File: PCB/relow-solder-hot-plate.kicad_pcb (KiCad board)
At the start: 2 copper layers, 100 x 100 mm, 57 parts, among them J1 Barrel_Jack_Switch, Q1 WSP4409A, Q2 IRLR8726TRPBF, Q3 SS8050, SW1 SW_Push, SW2 SW_Push, U1 ATMEGA4809-AFR, U2 AMS1117-5.0

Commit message: layout done
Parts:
- removed D4: B5819W, Diode_SMD:D_SOD-123
- removed LED1: RED/GREEN, LED_SMD:LED_Avago_PLCC4_3.2x2.8mm_CW
- removed OLED1: SSD1306, User:0.91Inch-OLED-Module
- removed R10: 4k7, Resistor_SMD:R_0805_2012Metric
- removed SW2: SW_Push, Button_Switch_THT:SW_PUSH_6mm
- removed TEMP3: Ext. 1-Wire, Connector_PinHeader_2.54mm:PinHeader_1x03_P2.54mm_Vertical
- removed UPDI1: 1x03_2.54mm, Connector_PinHeader_2.54mm:PinHeader_1x03_P2.54mm_Vertical
- added L1: 4.7u, Inductor_SMD:L_1210_3225Metric, F.Cu at (116.2, 68.2)
- added R16: 1K, Resistor_SMD:R_0603_1608Metric, F.Cu at (147.7, 65.8)
- added U3: ESP32-S3-MINI-1, Espressif:ESP32-S3-MINI-1, F.Cu at (131.6, 70.2)
- C1: value 10u -> 100n; footprint Capacitor_SMD:C_0805_2012Metric -> Capacitor_SMD:C_0603_1608Metric
- C10: value 100nF -> 10u; footprint Capacitor_SMD:C_0805_2012Metric -> Capacitor_SMD:C_0603_1608Metric
- C11, C12, C9: value 100nF -> 100n; footprint Capacitor_SMD:C_0805_2012Metric -> Capacitor_SMD:C_0603_1608Metric
- C13: value 100nF -> 68p; footprint Capacitor_SMD:C_0805_2012Metric -> Capacitor_SMD:C_0603_1608Metric
- C2: value 680u/16V -> 10u; footprint Capacitor_THT:CP_Radial_D8.0mm_P3.50mm -> Capacitor_SMD:C_0603_1608Metric
- C6: value 22u/16V -> 680u/16V; footprint Capacitor_SMD:CP_Elec_4x5.4 -> Capacitor_THT:CP_Radial_D8.0mm_P3.50mm
- C7: value 22u/16V -> 10u; footprint Capacitor_SMD:CP_Elec_4x5.4 -> Capacitor_SMD:C_0603_1608Metric
- C8: value 470pF -> 10u; footprint Capacitor_SMD:C_0805_2012Metric -> Capacitor_SMD:C_0603_1608Metric
- D3: value B5819W -> LED_RBAG; footprint Diode_SMD:D_SOD-123 -> LED_SMD:LED_Cree-PLCC4_2x2mm_CW
- F1: value 5A -> 3A
- J1: value Barrel_Jack_Switch -> USB_C_Receptacle; footprint Connector_BarrelJack:BarrelJack_Horizontal -> Connector_USB:USB_C_Receptacle_HRO_TYPE-C-31-M-12
- R1, R2: value 47 -> 100K; footprint Resistor_SMD:R_0805_2012Metric -> Resistor_SMD:R_0603_1608Metric
- R11: footprint Resistor_SMD:R_0805_2012Metric -> Resistor_SMD:R_0603_1608Metric
- R12: value 10k -> 1k; footprint Resistor_SMD:R_0805_2012Metric -> Resistor_SMD:R_0603_1608Metric
- R13: value 10k -> 10K; footprint Resistor_SMD:R_0805_2012Metric -> Resistor_SMD:R_0603_1608Metric
- R14, R15: value 10k -> 1K; footprint Resistor_SMD:R_0805_2012Metric -> Resistor_SMD:R_0603_1608Metric
- R3: value 1k -> 10K; footprint Resistor_SMD:R_0805_2012Metric -> Resistor_SMD:R_0603_1608Metric
- R4: value 4k7 -> 22K; footprint Resistor_SMD:R_0805_2012Metric -> Resistor_SMD:R_0603_1608Metric
- R5, R6: value 1k -> 5K1; footprint Resistor_SMD:R_0805_2012Metric -> Resistor_SMD:R_0603_1608Metric
- R7: value 1k -> 200K; footprint Resistor_SMD:R_0805_2012Metric -> Resistor_SMD:R_0603_1608Metric
- R8: value 4k7 -> 1K; footprint Resistor_SMD:R_0805_2012Metric -> Resistor_SMD:R_0603_1608Metric
- R9: value 4k7 -> 5K1; footprint Resistor_SMD:R_0805_2012Metric -> Resistor_SMD:R_0603_1608Metric
- SW1: footprint Button_Switch_THT:SW_PUSH_6mm -> Button_Switch_THT:SW_PUSH_6mm_H4.3mm
- TEMP2: value DS18B20Z -> LMT85; footprint Package_SO:SOIC-8_3.9x4.9mm_P1.27mm -> Package_SO:Texas_R-PDSO-N5
- U1: value ATMEGA4809-AFR -> DIO6912; footprint Package_QFP:TQFP-48_7x7mm_P0.5mm -> Package_TO_SOT_SMD:SOT-23-6
- U2: value AMS1117-5.0 -> IP2721; footprint Package_TO_SOT_SMD:SOT-89-3 -> Package_SO:TSSOP-16_4.4x5mm_P0.65mm
- moved R7 95.5 mm to (62.6, 69.6)
- moved R6 90.6 mm to (64.2, 73.0), turned to 90 degrees
- moved R5 66.2 mm to (62.6, 73.0), turned to 90 degrees
- moved R2 56.2 mm to (120.6, 62.8), turned to 90 degrees
- moved C1 53.6 mm to (115.4, 65.6), turned to 0 degrees
- moved U2 53.1 mm to (72.0, 74.0), turned to 180 degrees
- moved R11 48.3 mm to (110.6, 71.6), turned to 0 degrees
- moved R3 48.0 mm to (65.8, 69.6), turned to -90 degrees
- moved C6 30.6 mm to (88.1, 66.3), turned to 90 degrees
- moved C13 28.7 mm to (155.8, 94.0), turned to 180 degrees
- moved R13 28.4 mm to (150.8, 75.6), turned to 90 degrees
- moved D3 24.7 mm to (149.2, 62.5), turned to 180 degrees
- moved C2 23.9 mm to (64.2, 69.6)
- moved C8 22.0 mm to (119.8, 68.2), turned to 90 degrees
- moved U1 19.6 mm to (116.0, 63.0), turned to 180 degrees
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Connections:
- C10 pad 1: /SW_UP -> GND
- C10 pad 2: GND -> +3V3
- C11 pad 1: +5V -> GND
- C11 pad 2: GND -> +3V3
- C12 pad 1: /SW_DN -> GND
- C12 pad 2: GND -> /GPIO_0/BOOT
- C13 pad 1: +5V -> GND
- C13 pad 2: GND -> /T_ANALOG
- C2 pad 1: VCC -> Net-(C2-Pad1)
- C2 pad 2: GND -> Net-(C2-Pad2)
- C6 pad 1: Net-(C6-Pad1) -> VCC
- C7 pad 1: +5V -> GND
- C7 pad 2: GND -> Net-(C7-Pad2)
- C8 pad 1: /TDATA_A -> GND
- C8 pad 2: GND -> +3V3
- C9 pad 1: +5V -> GND
- C9 pad 2: GND -> Net-(C9-Pad2)
- D1 pad 1: Net-(C6-Pad1) -> Net-(C7-Pad2)
- D3 pad 1: Net-(C6-Pad1) -> Net-(D3-Pad1)
- D3 pad 2: +5V -> Net-(D3-Pad2)
- F1 pad 2: Net-(C1-Pad1) -> Net-(C2-Pad2)
- Q1 pad 4: Net-(C1-Pad2) -> Net-(C2-Pad1)
- Q1 pad 5: Net-(C1-Pad1) -> Net-(C2-Pad2)
- Q1 pad 6: Net-(C1-Pad1) -> Net-(C2-Pad2)
- Q1 pad 7: Net-(C1-Pad1) -> Net-(C2-Pad2)
- Q1 pad 8: Net-(C1-Pad1) -> Net-(C2-Pad2)
- R1 pad 1: Net-(J1-Pad3) -> VCC
- R1 pad 2: Net-(C1-Pad1) -> /SEL
- R11 pad 1: Net-(C1-Pad2) -> Net-(Q3-Pad1)
- R11 pad 2: GND -> +3V3
- R12 pad 1: Net-(C6-Pad1) -> /GATE
- R12 pad 2: /VCC-DIV -> Net-(Q3-Pad1)
- R13 pad 1: Net-(Q3-Pad1) -> +3V3
- R13 pad 2: +5V -> /GPIO_0/BOOT
- R14 pad 1: /SW_UP -> /LED_R
- R14 pad 2: +5V -> Net-(D3-Pad1)
- R15 pad 1: /SW_DN -> Net-(D3-Pad4)
- R15 pad 2: +5V -> /LED_G
- R2 pad 1: Net-(J1-Pad3) -> +3V3
- R2 pad 2: VCC -> Net-(R2-Pad2)
- R3 pad 1: /VCC-DIV -> Net-(C2-Pad2)
- R4 pad 1: Net-(Q2-Pad1) -> Net-(R2-Pad2)
- R4 pad 2: VCC -> GND
- R5 pad 1: /GATE -> /CC1
- R5 pad 2: Net-(Q3-Pad1) -> GND
- R6 pad 1: /LED_G -> /CC2
- R6 pad 2: Net-(LED1-Pad3) -> GND
- R7 pad 1: /LED_R -> Net-(C2-Pad1)
- R7 pad 2: Net-(LED1-Pad1) -> GND
- R8 pad 1: +5V -> Net-(C9-Pad2)
- R8 pad 2: /I2C_SDA -> +3V3
- R9 pad 1: +5V -> VCC
- R9 pad 2: /I2C_SCL -> Net-(Q2-Pad1)
- SW1 pad 1: /SW_UP -> /GPIO_0/BOOT
- TEMP1 pad 1: +5V -> +3V3
- TEMP1 pad 2: /TDATA_A -> /T_ANALOG
- TEMP2 pad 1: unconnected-(TEMP2-Pad1) -> +3V3
- TEMP2 pad 2: unconnected-(TEMP2-Pad2) -> /T_ANALOG
- TEMP2 pad 3: +5V -> GND
- TEMP2 pad 4: /TDATA_D -> (no net)
- TEMP2 pad 5: GND -> (no net)
- U1 pad 1: unconnected-(U1-Pad1) -> Net-(C1-Pad2)
- U1 pad 2: unconnected-(U1-Pad2) -> GND
- U1 pad 3: unconnected-(U1-Pad3) -> Net-(R2-Pad2)
- U1 pad 4: unconnected-(U1-Pad4) -> Net-(C7-Pad2)
- U1 pad 5: unconnected-(U1-Pad5) -> Net-(C7-Pad2)
- U1 pad 6: unconnected-(U1-Pad6) -> Net-(C1-Pad1)
- U2 pad 1: GND -> unconnected-(U2-Pad1)
- U2 pad 2: +5V -> VCC
- U2 pad 3: Net-(C6-Pad1) -> unconnected-(U2-Pad3)
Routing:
- net +5V: track 131.9 -> 0.00 mm, vias 2 -> 0
- net +3V3: track 0.00 -> 73.0 mm
- net /D+: track 0.00 -> 65.1 mm, vias 0 -> 2
- net /D-: track 0.00 -> 62.6 mm, vias 0 -> 2
- net /T_ANALOG: track 0.00 -> 59.0 mm
- net /TDATA_D: track 55.1 -> 0.00 mm, vias 4 -> 0
- net GND: track 68.4 -> 22.4 mm, vias 58 -> 65
- net /I2C_SCL: track 44.3 -> 0.00 mm, vias 2 -> 0
- net /TDATA_A: track 41.0 -> 0.00 mm, vias 3 -> 0
- net /I2C_SDA: track 35.0 -> 0.00 mm, vias 2 -> 0
- net Net-(C1-Pad1): track 32.7 -> 0.00 mm
- net /GPIO_0/BOOT: track 0.00 -> 32.0 mm
- net /VCC-DIV: track 30.6 -> 0.00 mm, vias 4 -> 0
- net /UPDI: track 29.0 -> 0.00 mm, vias 2 -> 0
- net /LED_B: track 0.00 -> 21.9 mm, vias 0 -> 2
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- added copper zone on F.Cu, net +3V3
- added copper zone on F.Cu, net Net-(C1-Pad2)
- added copper zone on F.Cu, net Net-(C2-Pad1)
- added copper zone on F.Cu, net Net-(C2-Pad2)
- added copper zone on F.Cu, net Net-(C7-Pad2)
- removed copper zone on F.Cu, net +5V
- removed copper zone on F.Cu, net Net-(C6-Pad1)
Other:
- board text added: "20V/3A min"
- board text added: "Ver 1.0 - 0123"
- board text added: "github.com/LDAB"
- board text removed: "+5V"
- board text removed: "12V/5A min"
- board text removed: "DQ"
- board text removed: "JLCJLCJLCJLC"
- board text removed: "UPDI"
- board text removed: "Ver 1.1"
- board text removed: "github.com/DerSpatz/PCB-reflow-solder-heat-plate development by: Bastian Mohing (hardware) Nathan Heidt (software) Merlin Shaw (testing)"

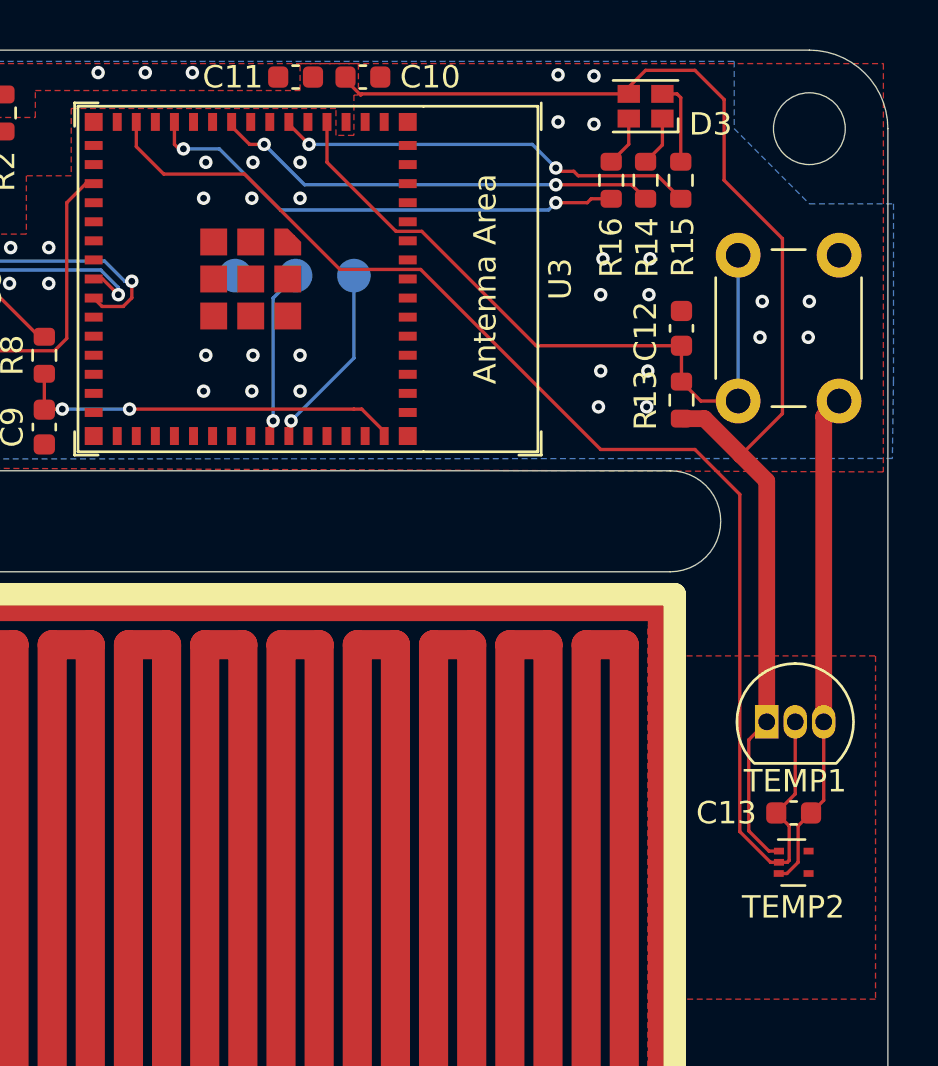
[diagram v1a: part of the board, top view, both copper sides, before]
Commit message: Proto (#2)
* FW draft

* web server

* draft gpios

* lmt85

* draft temp control

* dry run

* minor fix

* LEDs are active LOW

* inverted PWM

* captive portal and webserver

* Fix silkscreen and LMT85 footprint

* fix adc attenuation

* fix pwm frequency

* minor fix

* proto

* lmt85 fix

* create mdns task

* green led when connected

* reset leds, when color changes

* 20V@2.25A power supply

* wet run

* fix mdns

* PID
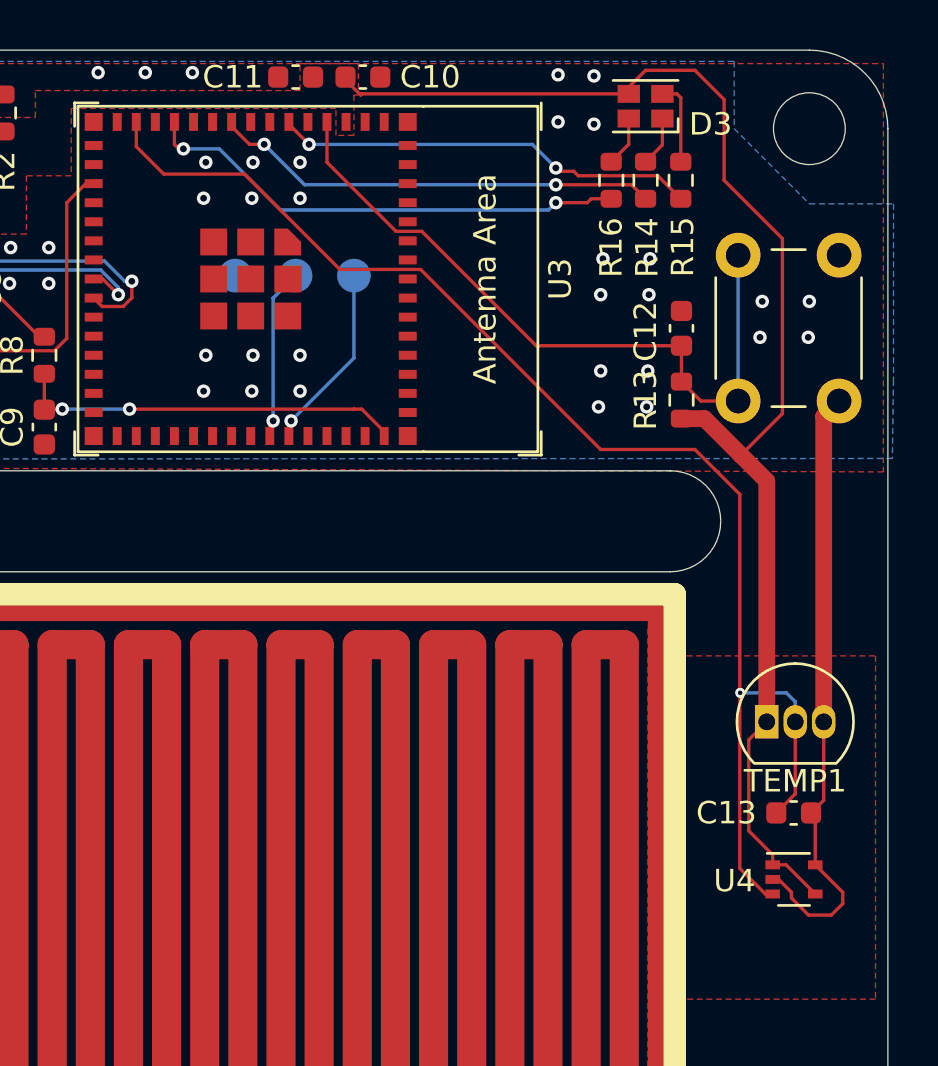
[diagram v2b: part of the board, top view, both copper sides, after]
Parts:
- removed TEMP2: LMT85, Package_SO:Texas_R-PDSO-N5
- added U4: LMT85DCK, Package_TO_SOT_SMD:SOT-353_SC-70-5, F.Cu at (155.8, 97.0)
- R7: value 200K -> 1M
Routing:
- net GND: track 22.4 -> 27.6 mm
- net +3V3: track 73.0 -> 75.7 mm
- net /T_ANALOG: track 59.0 -> 61.0 mm, vias 0 -> 1

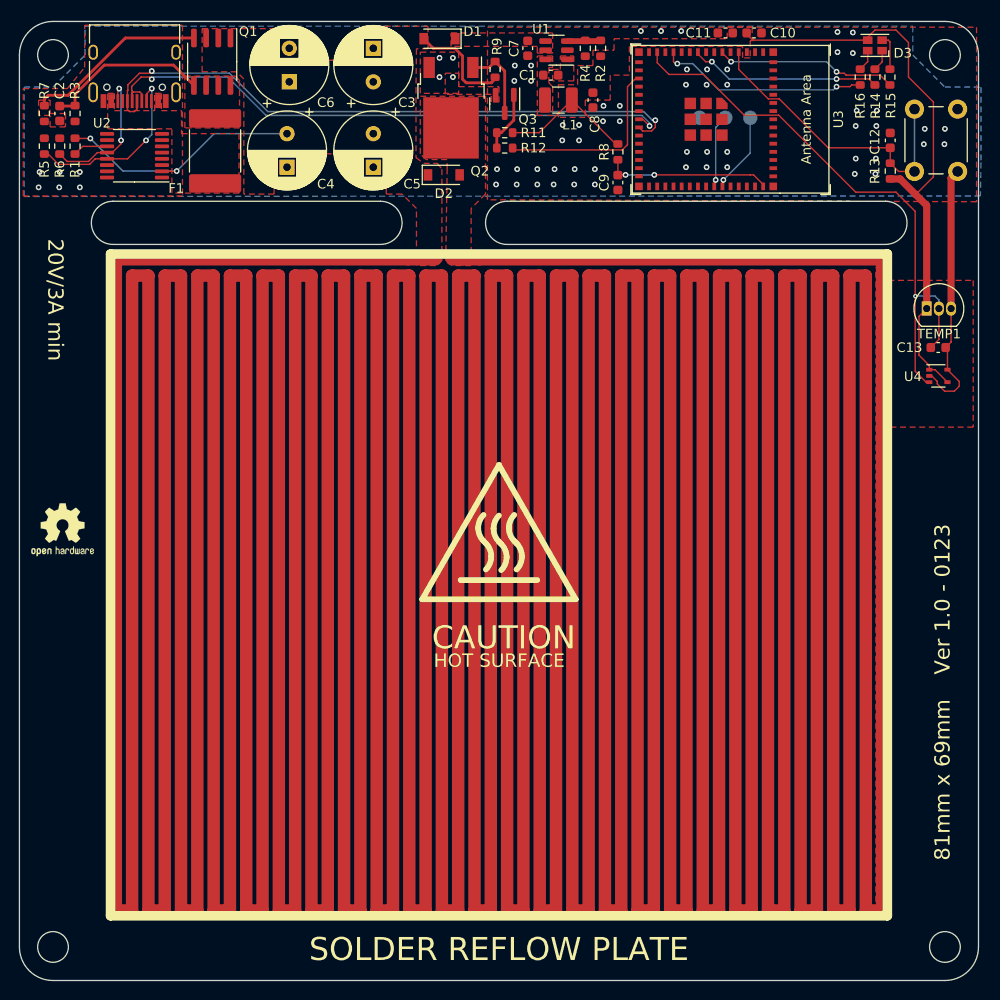
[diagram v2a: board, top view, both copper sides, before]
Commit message: fix usb-c programmer
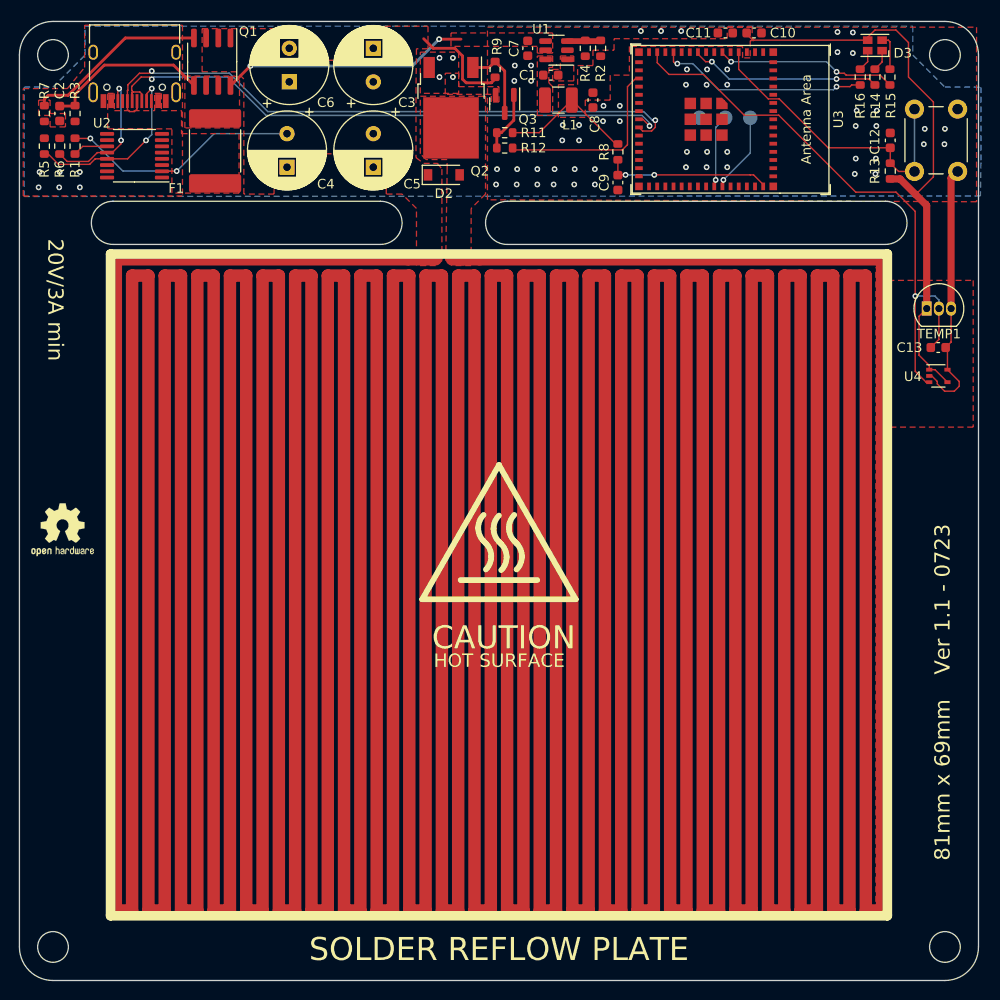
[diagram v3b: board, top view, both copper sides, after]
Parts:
- removed D1: B5819W, Diode_SMD:D_SOD-123
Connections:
- C2 pad 2: Net-(C2-Pad2) -> +5V
- C7 pad 2: Net-(D1-K) -> +5V
- F1 pad 2: Net-(C2-Pad2) -> +5V
- Q1 pad 5: Net-(C2-Pad2) -> +5V
- Q1 pad 6: Net-(C2-Pad2) -> +5V
- Q1 pad 7: Net-(C2-Pad2) -> +5V
- Q1 pad 8: Net-(C2-Pad2) -> +5V
- R3 pad 1: Net-(C2-Pad2) -> +5V
- U1 pad 4: Net-(D1-K) -> +5V
- U1 pad 5: Net-(D1-K) -> +5V
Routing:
- net +5V: track 0.00 -> 43.4 mm, vias 0 -> 2
- net Net-(C2-Pad2): track 17.3 -> 0.00 mm
- added copper zone on F.Cu, net +5V
- removed copper zone on F.Cu, net Net-(C2-Pad2)
- removed copper zone on F.Cu, net Net-(D1-K)
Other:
- board text added: "Ver 1.1 - 0723"
- board text removed: "Ver 1.0 - 0123"
